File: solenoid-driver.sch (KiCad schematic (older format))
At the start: 0 parts

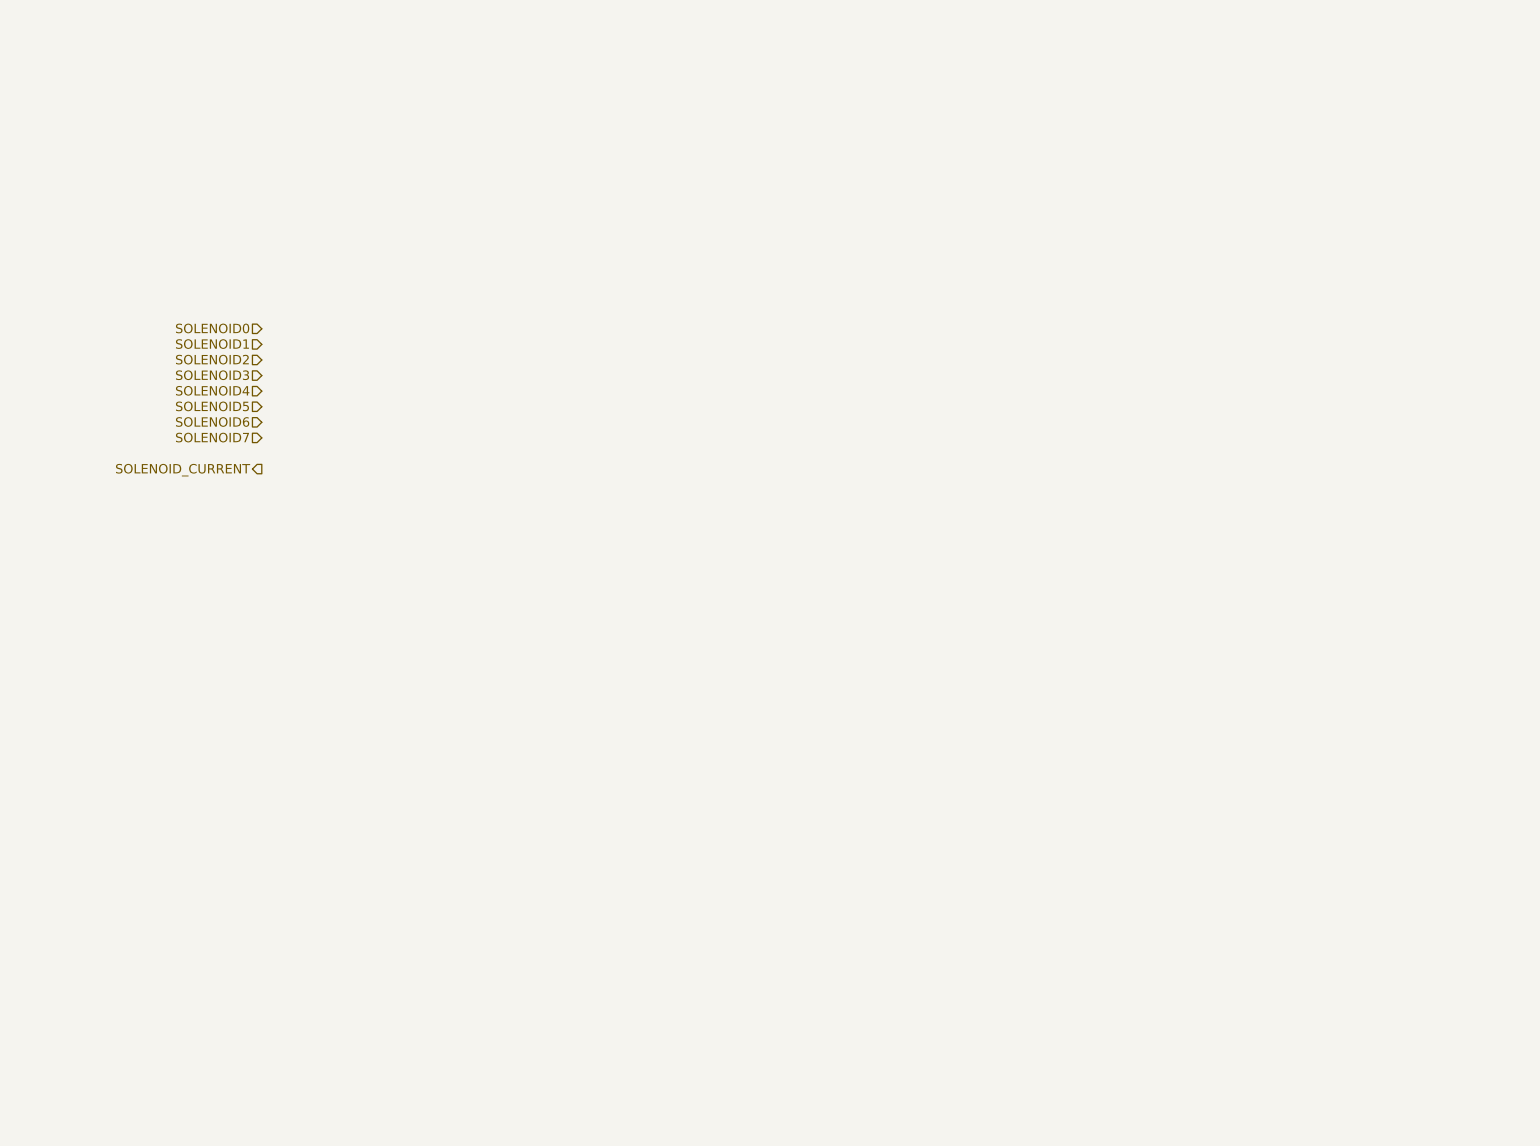
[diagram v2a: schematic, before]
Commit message: Added library for custom parts Switch matrix and solenoid driver mostly done
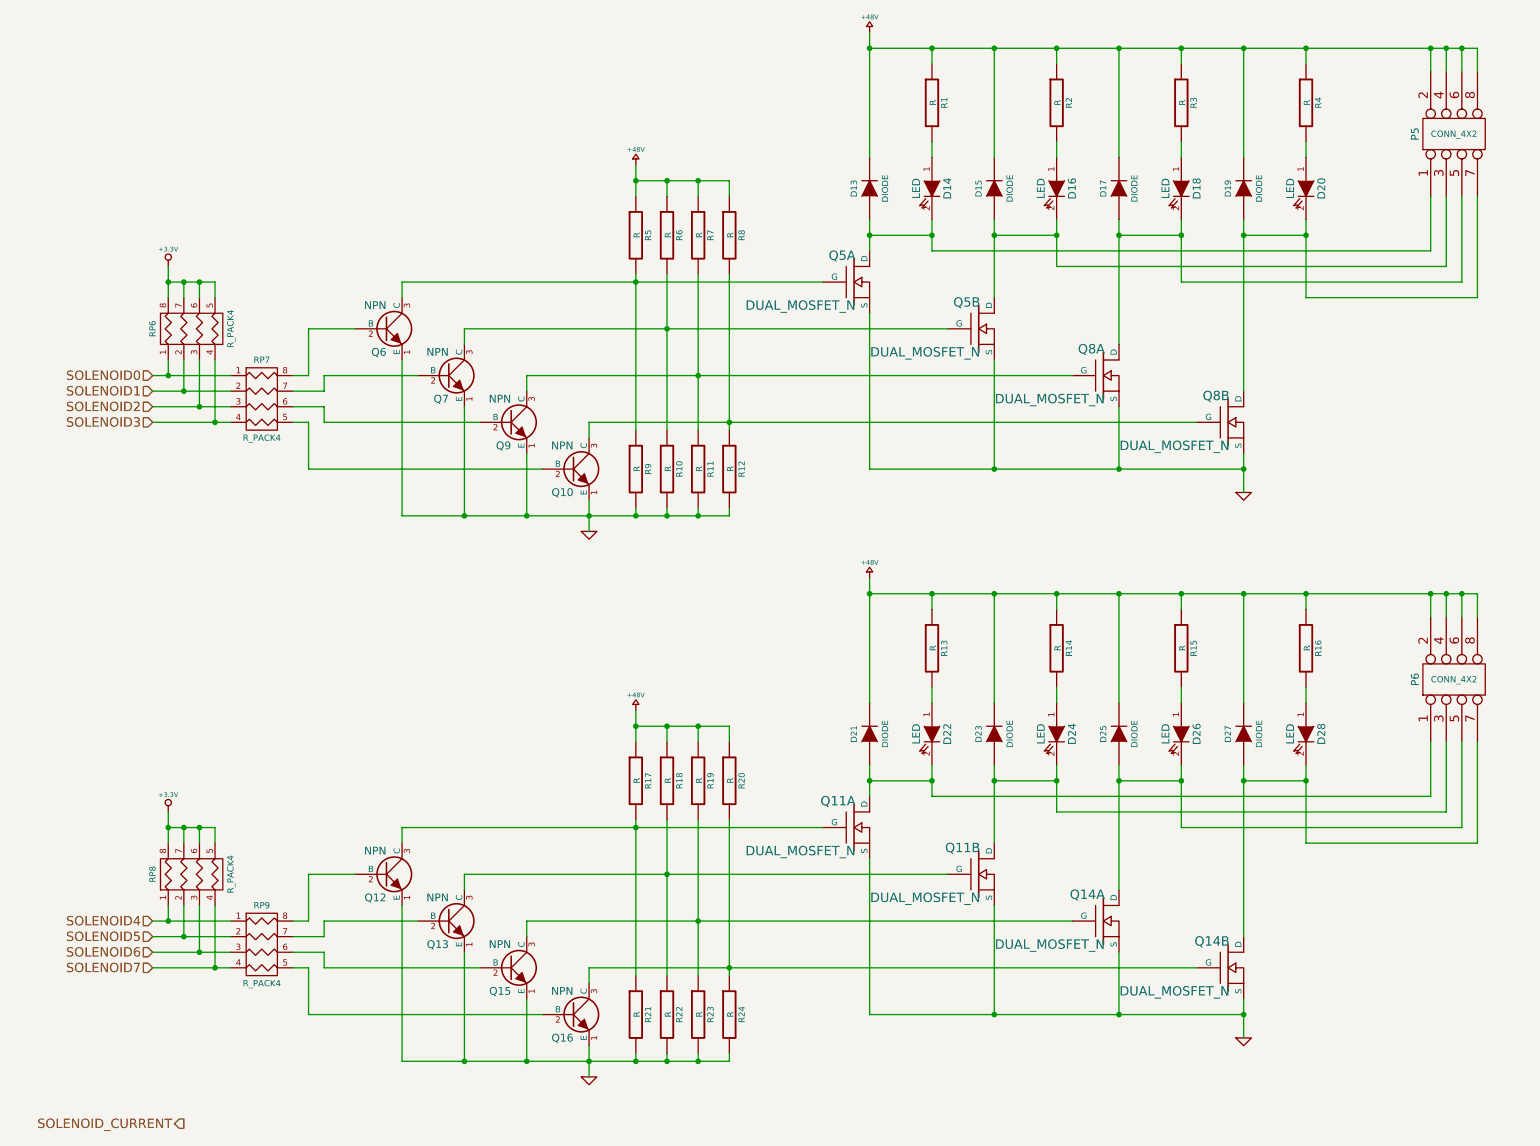
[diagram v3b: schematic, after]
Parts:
- added D13, D15, D17, D19, D21, D23, D25, D27: DIODE, ~, symbol DIODE
- added D14, D16, D18, D20, D22, D24, D26, D28: LED, ~, symbol LED
- added P5, P6: CONN_4X2, symbol CONN_4X2
- added Q10, Q12, Q13, Q15, Q16, Q6, Q7, Q9: NPN, ~, symbol NPN
- added Q11, Q14, Q5, Q8: DUAL_MOSFET_N, ~, symbol DUAL_MOSFET_N
- added R1, R10, R11, R12, R13, R14, R15, R16, R17, R18, R19, R2, R20, R21, R22, R23, R24, R3, R4, R5, R6, R7, R8, R9: R, ~, symbol R
- added RP6, RP7, RP8, RP9: R_PACK4, ~, symbol R_PACK4
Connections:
- net SOLENOID0: now also RP6.1 (P1), RP7.1 (P1)
- net SOLENOID1: now also RP6.2 (P2), RP7.2 (P2)
- net SOLENOID2: now also RP6.3 (P3), RP7.3 (P3)
- net SOLENOID3: now also RP6.4 (P4), RP7.4 (P4)
- net SOLENOID4: now also RP8.1 (P1), RP9.1 (P1)
- net SOLENOID5: now also RP8.2 (P2), RP9.2 (P2)
- net SOLENOID6: now also RP8.3 (P3), RP9.3 (P3)
- net SOLENOID7: now also RP8.4 (P4), RP9.4 (P4)
- new net: Q12.2 (B), RP9.8 (R1)
- new net: Q11.G1 (G), Q12.3 (C), R17.2, R21.1
- new net: Q16.2 (B), RP9.5 (R4)
- new net: Q15.2 (B), RP9.6 (R3)
- new net: Q13.2 (B), RP9.7 (R2)
- new net: D21.1 (A), D22.2 (K), P6.1, Q11.D1 (D)
- new net: Q11.G2 (G), Q13.3 (C), R18.2, R22.1
- new net: Q14.G1 (G), Q15.3 (C), R19.2, R23.1
- new net: Q14.G2 (G), Q16.3 (C), R20.2, R24.1
- new net: D23.1 (A), D24.2 (K), P6.3, Q11.D2 (D)
- new net: D25.1 (A), D26.2 (K), P6.5, Q14.D1 (D)
- new net: D27.1 (A), D28.2 (K), P6.7, Q14.D2 (D)
- new net: D22.1 (A), R13.2
- new net: D24.1 (A), R14.2
- new net: D26.1 (A), R15.2
- new net: D28.1 (A), R16.2
- new net: Q6.2 (B), RP7.8 (R1)
- new net: Q5.G1 (G), Q6.3 (C), R5.2, R9.1
- new net: Q10.2 (B), RP7.5 (R4)
- new net: Q9.2 (B), RP7.6 (R3)
- new net: Q7.2 (B), RP7.7 (R2)
- new net: D13.1 (A), D14.2 (K), P5.1, Q5.D1 (D)
- new net: Q5.G2 (G), Q7.3 (C), R10.1, R6.2
- new net: Q8.G1 (G), Q9.3 (C), R11.1, R7.2
- new net: Q10.3 (C), Q8.G2 (G), R12.1, R8.2
- new net: D15.1 (A), D16.2 (K), P5.3, Q5.D2 (D)
- new net: D17.1 (A), D18.2 (K), P5.5, Q8.D1 (D)
- new net: D19.1 (A), D20.2 (K), P5.7, Q8.D2 (D)
- new net: D14.1 (A), R1.2
- new net: D16.1 (A), R2.2
- new net: D18.1 (A), R3.2
- new net: D20.1 (A), R4.2
- new net +3.3V: RP6.5 (R4), RP6.6 (R3), RP6.7 (R2), RP6.8 (R1), RP8.5 (R4), RP8.6 (R3), RP8.7 (R2), RP8.8 (R1)
- new net +48V: D13.2 (K), D15.2 (K), D17.2 (K), D19.2 (K), D21.2 (K), D23.2 (K), D25.2 (K), D27.2 (K), P5.2, P5.4, P5.6, P5.8, P6.2, P6.4, P6.6, P6.8, R1.1, R13.1, R14.1, R15.1, R16.1, R17.1, R18.1, R19.1, R2.1, R20.1, R3.1, R4.1, R5.1, R6.1, R7.1, R8.1
- new net GND: Q10.1 (E), Q11.S1 (S), Q11.S2 (S), Q12.1 (E), Q13.1 (E), Q14.S1 (S), Q14.S2 (S), Q15.1 (E), Q16.1 (E), Q5.S1 (S), Q5.S2 (S), Q6.1 (E), Q7.1 (E), Q8.S1 (S), Q8.S2 (S), Q9.1 (E), R10.2, R11.2, R12.2, R21.2, R22.2, R23.2, R24.2, R9.2

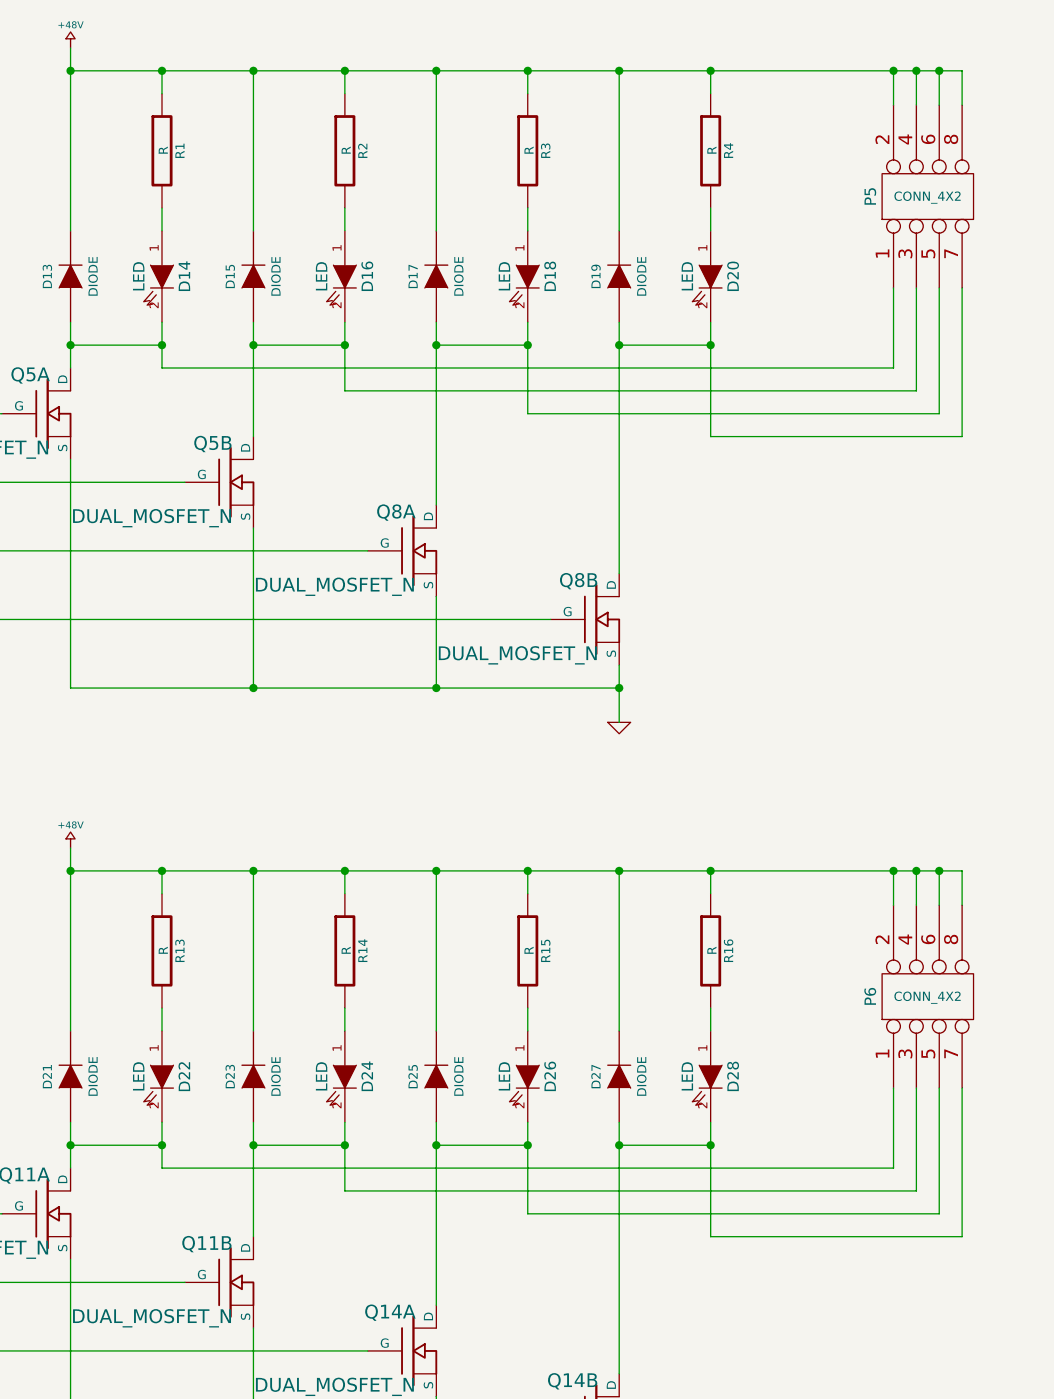
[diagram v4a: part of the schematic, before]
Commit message: Fixed switch matrix to match Mike's sketches Added lamp matrix
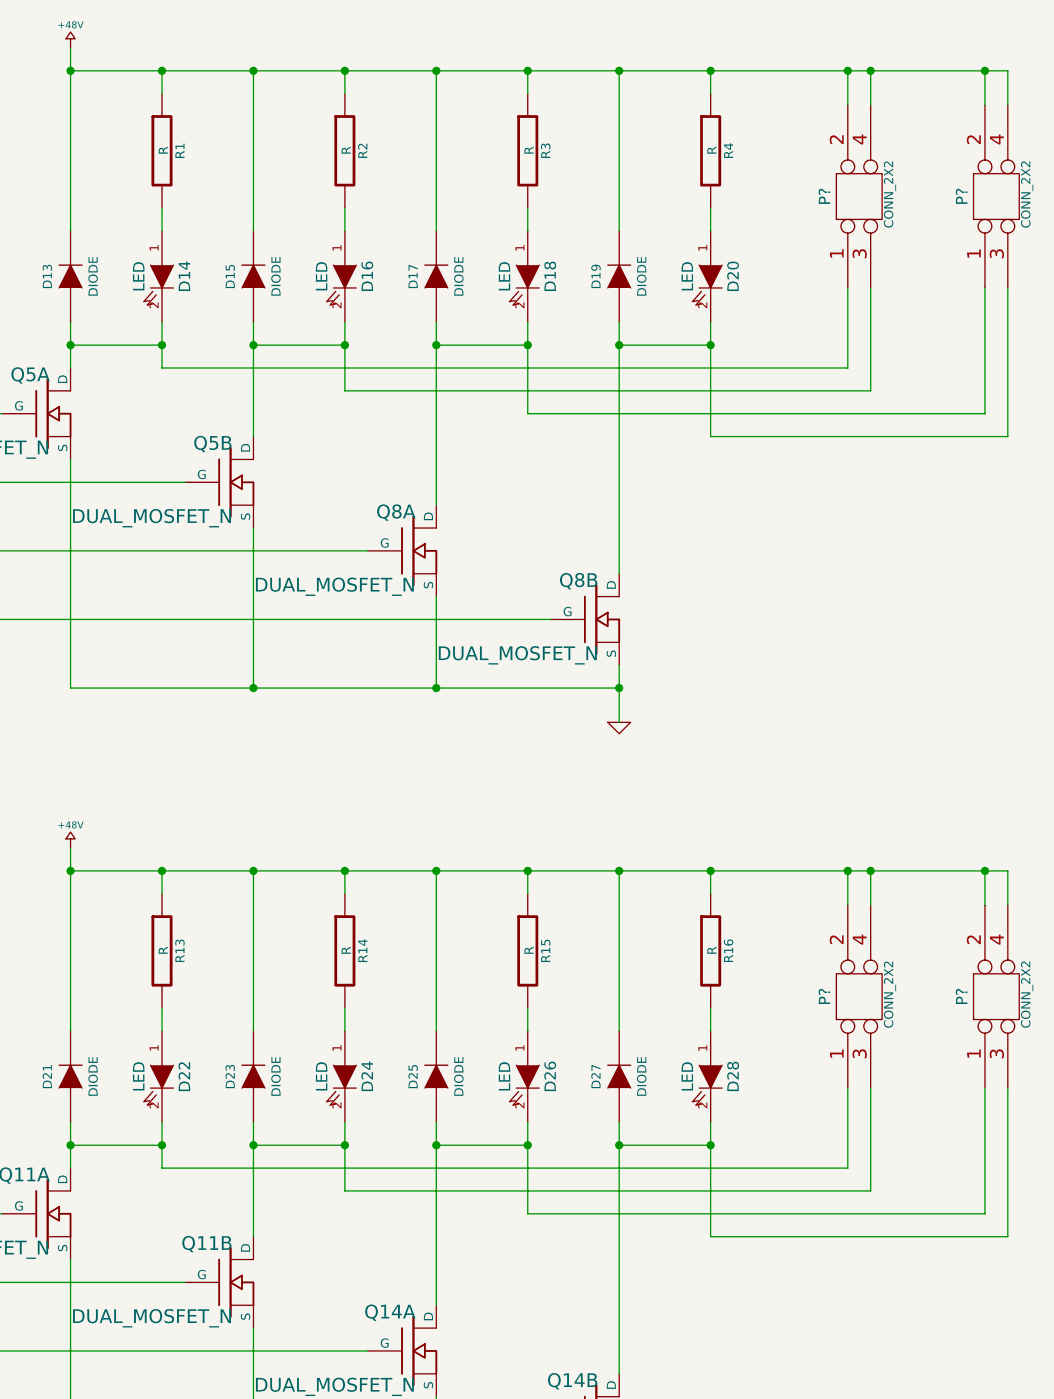
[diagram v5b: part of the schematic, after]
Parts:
- removed P5, P6: CONN_4X2, symbol CONN_4X2
- added P? (x4): CONN_2X2, symbol CONN_2X2
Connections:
- net +48V: now also P?.2, P?.2, P?.2, P?.2, P?.4, P?.4, P?.4, P?.4
- net at D21.1 (A), D22.2 (K), Q11.D1 (D): now also P?.1
- net at D23.1 (A), D24.2 (K), Q11.D2 (D): now also P?.3
- net at D25.1 (A), D26.2 (K), Q14.D1 (D): now also P?.1
- net at D27.1 (A), D28.2 (K), Q14.D2 (D): now also P?.3
- net at D13.1 (A), D14.2 (K), Q5.D1 (D): now also P?.1
- net at D15.1 (A), D16.2 (K), Q5.D2 (D): now also P?.3
- net at D17.1 (A), D18.2 (K), Q8.D1 (D): now also P?.1
- net at D19.1 (A), D20.2 (K), Q8.D2 (D): now also P?.3
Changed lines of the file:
@@
-EESchema Schematic File Version 2  date 4/10/2013 12:52:04 AM
+EESchema Schematic File Version 2  date 4/13/2013 6:56:07 PM
 LIBS:power
 LIBS:device
@@
 Sheet 5 5
 Title ""
-Date "10 apr 2013"
+Date "13 apr 2013"
 Rev ""
 Comp ""
@@
 	8400 4300 8800 4300
 Wire Wire Line
-	8800 4300 9600 4300
-Wire Wire Line
-	9600 4300 9700 4300
-Wire Wire Line
-	9700 4300 9800 4300
-Wire Wire Line
-	9800 4300 9900 4300
+	8800 4300 9400 4300
+Wire Wire Line
+	9400 4300 9500 4300
+Wire Wire Line
+	9500 4300 10000 4300
+Wire Wire Line
+	10000 4300 10100 4300
 Wire Wire Line
 	6000 4200 6000 4300
@@
 	8000 4400 8000 4300
 Connection ~ 8000 4300
-$Comp
-L CONN_4X2 P6
-U 1 1 5164FF40
-P 9750 4850
-F 0 "P6" H 9750 5100 50  0000 C CNN
-F 1 "CONN_4X2" V 9750 4850 40  0000 C CNN
-F 2 "" H 9750 4850 60  0000 C CNN
-F 3 "" H 9750 4850 60  0000 C CNN
-	1    9750 4850
-	0    -1   -1   0
-$EndComp
-Wire Wire Line
-	9900 4300 9900 4450
+Wire Wire Line
+	10100 4300 10100 4450
 Connection ~ 8800 4300
 Wire Wire Line
-	9800 4450 9800 4300
-Connection ~ 9800 4300
-Wire Wire Line
-	9700 4450 9700 4300
-Connection ~ 9700 4300
-Wire Wire Line
-	9600 4450 9600 4300
-Connection ~ 9600 4300
-Wire Wire Line
-	9600 5250 9600 5600
-Wire Wire Line
-	9600 5600 6400 5600
+	10000 4450 10000 4300
+Connection ~ 10000 4300
+Wire Wire Line
+	9500 4450 9500 4300
+Connection ~ 9500 4300
+Wire Wire Line
+	9400 4450 9400 4300
+Connection ~ 9400 4300
+Wire Wire Line
+	9400 5250 9400 5600
+Wire Wire Line
+	9400 5600 6400 5600
 Connection ~ 6400 5500
 Wire Wire Line
-	9700 5250 9700 5700
-Wire Wire Line
-	9700 5700 7200 5700
+	9500 5250 9500 5700
+Wire Wire Line
+	9500 5700 7200 5700
 Connection ~ 7200 5500
 Wire Wire Line
-	9800 5250 9800 5800
-Wire Wire Line
-	9800 5800 8000 5800
+	10000 5250 10000 5800
+Wire Wire Line
+	10000 5800 8000 5800
 Connection ~ 8000 5500
 Wire Wire Line
-	9900 5250 9900 5900
-Wire Wire Line
-	9900 5900 8800 5900
+	10100 5250 10100 5900
+Wire Wire Line
+	10100 5900 8800 5900
 Connection ~ 8800 5500
 $Comp
@@
 	8400 800  8800 800
 Wire Wire Line
-	8800 800  9600 800
-Wire Wire Line
-	9600 800  9700 800
-Wire Wire Line
-	9700 800  9800 800
-Wire Wire Line
-	9800 800  9900 800
+	8800 800  9400 800
+Wire Wire Line
+	9400 800  9500 800
+Wire Wire Line
+	9500 800  10000 800
+Wire Wire Line
+	10000 800  10100 800
 Wire Wire Line
 	6000 700  6000 800
@@
 	8000 900  8000 800
 Connection ~ 8000 800
-$Comp
-L CONN_4X2 P5
-U 1 1 516504CA
-P 9750 1350
-F 0 "P5" H 9750 1600 50  0000 C CNN
-F 1 "CONN_4X2" V 9750 1350 40  0000 C CNN
-F 2 "" H 9750 1350 60  0000 C CNN
-F 3 "" H 9750 1350 60  0000 C CNN
-	1    9750 1350
-	0    -1   -1   0
-$EndComp
-Wire Wire Line
-	9900 800  9900 950
+Wire Wire Line
+	10100 800  10100 950
 Connection ~ 8800 800
 Wire Wire Line
-	9800 950  9800 800
-Connection ~ 9800 800
-Wire Wire Line
-	9700 950  9700 800
-Connection ~ 9700 800
-Wire Wire Line
-	9600 950  9600 800
-Connection ~ 9600 800
-Wire Wire Line
-	9600 1750 9600 2100
-Wire Wire Line
-	9600 2100 6400 2100
+	10000 950  10000 800
+Connection ~ 10000 800
+Wire Wire Line
+	9500 950  9500 800
+Connection ~ 9500 800
+Wire Wire Line
+	9400 950  9400 800
+Connection ~ 9400 800
+Wire Wire Line
+	9400 1750 9400 2100
+Wire Wire Line
+	9400 2100 6400 2100
 Connection ~ 6400 2000
 Wire Wire Line
-	9700 1750 9700 2200
-Wire Wire Line
-	9700 2200 7200 2200
+	9500 1750 9500 2200
+Wire Wire Line
+	9500 2200 7200 2200
 Connection ~ 7200 2000
 Wire Wire Line
-	9800 1750 9800 2300
-Wire Wire Line
-	9800 2300 8000 2300
+	10000 1750 10000 2300
+Wire Wire Line
+	10000 2300 8000 2300
 Connection ~ 8000 2000
 Wire Wire Line
-	9900 1750 9900 2400
-Wire Wire Line
-	9900 2400 8800 2400
+	10100 1750 10100 2400
+Wire Wire Line
+	10100 2400 8800 2400
 Connection ~ 8800 2000
 $Comp
@@
 Connection ~ 1700 6600
 Connection ~ 1800 6700
+$Comp
+L CONN_2X2 P?
+U 1 1 516A1DB4
+P 9450 1350
+F 0 "P?" H 9450 1500 50  0000 C CNN
+F 1 "CONN_2X2" H 9460 1220 40  0000 C CNN
+F 2 "" H 9450 1350 60  0000 C CNN
+F 3 "" H 9450 1350 60  0000 C CNN
+	1    9450 1350
+	0    -1   -1   0
+$EndComp
+$Comp
+L CONN_2X2 P?
+U 1 1 516A1DC3
+P 10050 1350
+F 0 "P?" H 10050 1500 50  0000 C CNN
+F 1 "CONN_2X2" H 10060 1220 40  0000 C CNN
+F 2 "" H 10050 1350 60  0000 C CNN
+F 3 "" H 10050 1350 60  0000 C CNN
+	1    10050 1350
+	0    -1   -1   0
+$EndComp
+$Comp
+L CONN_2X2 P?
+U 1 1 516A1DD2
+P 9450 4850
+F 0 "P?" H 9450 5000 50  0000 C CNN
+F 1 "CONN_2X2" H 9460 4720 40  0000 C CNN
+F 2 "" H 9450 4850 60  0000 C CNN
+F 3 "" H 9450 4850 60  0000 C CNN
+	1    9450 4850
+	0    -1   -1   0
+$EndComp
+$Comp
+L CONN_2X2 P?
+U 1 1 516A1DE1
+P 10050 4850
+F 0 "P?" H 10050 5000 50  0000 C CNN
+F 1 "CONN_2X2" H 10060 4720 40  0000 C CNN
+F 2 "" H 10050 4850 60  0000 C CNN
+F 3 "" H 10050 4850 60  0000 C CNN
+	1    10050 4850
+	0    -1   -1   0
+$EndComp
 $EndSCHEMATC
